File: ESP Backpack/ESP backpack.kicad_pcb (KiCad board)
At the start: 2 copper layers, 100 x 100 mm, 37 parts, among them J1 HLE-120-02-F-DV-BE-K, J2 HLE-120-02-F-DV-BE-K, U1 ESP32-DEVKITC-32D, U2 VCNL4010-GS08

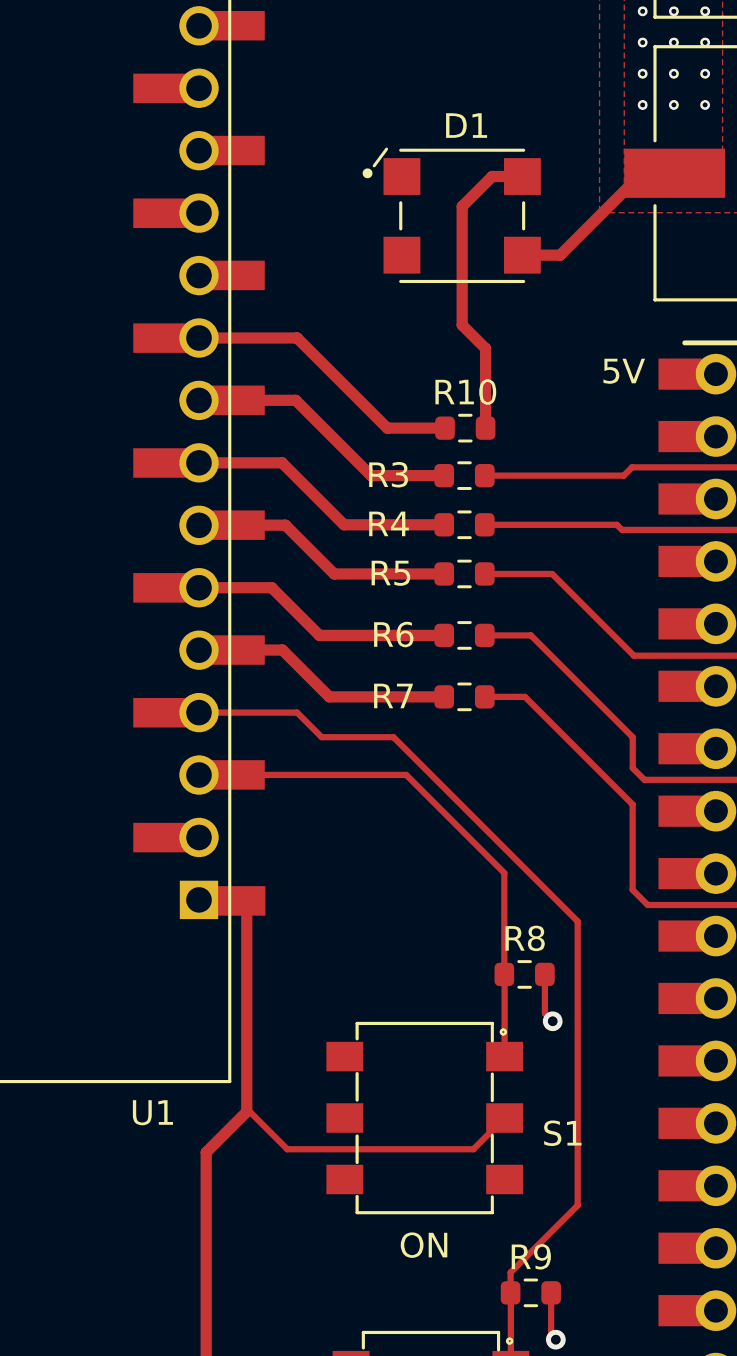
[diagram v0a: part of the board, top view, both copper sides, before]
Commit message: Re-org files for relative pathing, change extensions for globally unique names
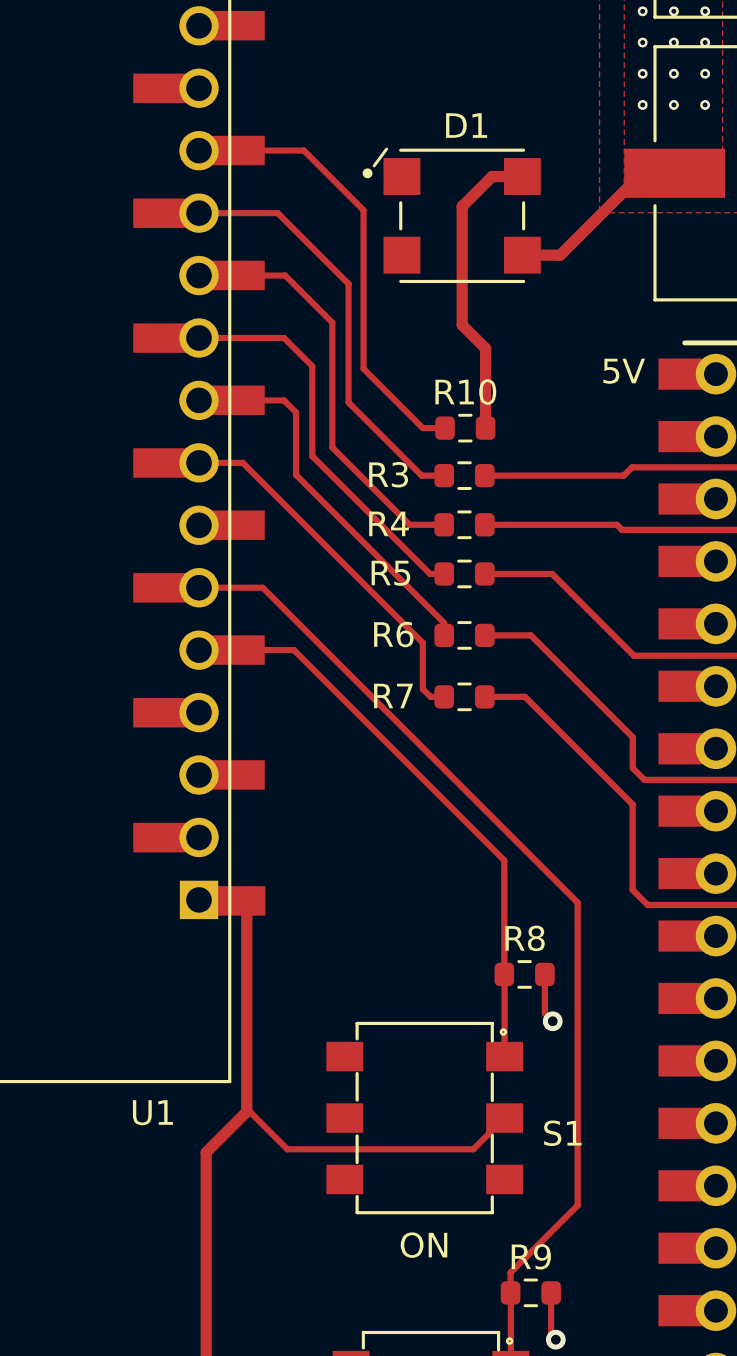
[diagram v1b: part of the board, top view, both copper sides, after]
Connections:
- D1 pad 2: Net-(D1-Pad2) -> (no net)
- J1 pad 30: GND -> Net-(J1-Pad30)
- J1 pad 34: GND -> Net-(J1-Pad34)
- J1 pad 38: GND -> Net-(J1-Pad38)
- J2 pad 29: +5V -> Net-(J2-Pad29)
- S1 pad 3: Net-(S1-Pad3) -> (no net)
- S1 pad 4: Net-(S1-Pad4) -> (no net)
- S1 pad 5: Net-(S1-Pad5) -> (no net)
- S1 pad 6: Net-(S1-Pad6) -> (no net)
- S2 pad 3: Net-(S2-Pad3) -> (no net)
- S2 pad 4: Net-(S2-Pad4) -> (no net)
- S2 pad 5: Net-(S2-Pad5) -> (no net)
- S2 pad 6: Net-(S2-Pad6) -> (no net)
- U1 pad 10: Net-(R10-Pad1) -> Net-(R5-Pad1)
- U1 pad 11: Net-(U1-Pad11) -> Net-(R4-Pad1)
- U1 pad 12: Net-(U1-Pad12) -> Net-(R3-Pad1)
- U1 pad 13: Net-(U1-Pad13) -> Net-(R10-Pad1)
- U1 pad 3: Net-(R8-Pad1) -> Net-(U1-Pad3)
- U1 pad 4: Net-(R9-Pad1) -> Net-(U1-Pad4)
- U1 pad 5: Net-(R7-Pad1) -> Net-(R8-Pad1)
- U1 pad 6: Net-(R6-Pad1) -> Net-(R9-Pad1)
- U1 pad 7: Net-(R5-Pad1) -> Net-(U1-Pad7)
- U1 pad 8: Net-(R4-Pad1) -> Net-(R7-Pad1)
- U1 pad 9: Net-(R3-Pad1) -> Net-(R6-Pad1)
- U2 pad 10: Net-(U2-Pad10) -> (no net)
- U2 pad 11: Net-(U2-Pad11) -> (no net)
- U2 pad 2: Net-(U2-Pad2) -> (no net)
- U2 pad 3: Net-(U2-Pad3) -> (no net)
- U2 pad 6: Net-(U2-Pad6) -> (no net)
- U2 pad 8: Net-(U2-Pad8) -> (no net)
- U2 pad 9: Net-(U2-Pad9) -> (no net)
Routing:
- net Net-(R3-Pad1): track 9.64 -> 18.8 mm
- net Net-(R5-Pad1): track 9.20 -> 17.7 mm
- net Net-(R7-Pad1): track 9.16 -> 16.6 mm
- net Net-(R10-Pad1): track 11.5 -> 18.5 mm
- net Net-(R4-Pad1): track 11.0 -> 17.2 mm
- net Net-(R6-Pad1): track 10.8 -> 15.7 mm
- net Net-(R9-Pad1): track 38.1 -> 42.3 mm
- net Net-(R8-Pad1): track 19.9 -> 22.3 mm
- net Net-(J1-Pad34): track 0.00 -> 1.41 mm
- net GND: track 31.6 -> 30.2 mm
